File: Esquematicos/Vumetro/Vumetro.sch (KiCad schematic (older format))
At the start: 13 parts

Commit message: actualización esquemático matriz de led y driver
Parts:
- removed J?: AudioJack3_Ground, symbol Connector:AudioJack3_Ground
- added C?: 1.0uF, symbol pspice:CAP
- added C?: 0.1uF, symbol pspice:CAP
- added J?: AudioJack5_Ground, symbol Connector:AudioJack5_Ground
- added R?: 10K, symbol Device:R
- U?: symbol vumetro:MAX7219 -> Vumetro-rescue:MAX7219-vumetro
- U? (x2): symbol vumetro:conn_pin8 -> Vumetro-rescue:conn_pin8-vumetro
- U?: symbol vumetro:opa2350pa -> Vumetro-rescue:opa2350pa-vumetro
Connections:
- net labels added: +5V, DIC0, DIC1, DIC2, DIC3, DIC4, DIC5, DIC6, DIC7, GND, ISET, SEGA, SEGB, SEGC, SEGD, SEGDP, SEGE, SEGF, SEGG, SPI_MOSI, SPI_SCK, V+
- wire segments 33 -> 105
- no-connect marks 4 -> 9
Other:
- moved on the sheet: C1, C2, R1, R2, R?, RV?, U?

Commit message: esquematico final
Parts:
- removed U?: MAX7219, symbol Vumetro-rescue:MAX7219-vumetro
- added P1, P2: conn_pin40, symbol vumetro:conn_pin40
- added U1: MAX7219, symbol vumetro:MAX7219
- U2, U3: renamed from U?; symbol Vumetro-rescue:conn_pin8-vumetro -> Vumetro-rescue:conn_pin8-vumetro-Vumetro-rescue
- U4: renamed from U?; symbol Vumetro-rescue:opa2350pa-vumetro -> Vumetro-rescue:opa2350pa-vumetro-Vumetro-rescue
- gave numbers to parts that had none: 8
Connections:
- net labels added: 3V3, 5V, CH1, VCC
- net labels removed: ADC
- wire segments 105 -> 136
- no-connect marks 9 -> 55

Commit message: perdon capitan
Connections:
- net labels added: +3V3
- net labels removed: +3.3V, VCC
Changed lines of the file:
@@
 $EndComp
-$Comp
-L power:+3.3V #PWR0101
-U 1 1 5BD083BF
-P 3350 2050
-F 0 "#PWR0101" H 3350 1900 50  0001 C CNN
-F 1 "+3.3V" H 3365 2223 50  0000 C CNN
-F 2 "" H 3350 2050 50  0001 C CNN
-F 3 "" H 3350 2050 50  0001 C CNN
-	1    3350 2050
-	1    0    0    -1
-$EndComp
-Wire Wire Line
-	3350 2050 3350 2250
 $Comp
 L power:GNDA #PWR0102
@@
 	1    0    0    -1
 $EndComp
-$Comp
-L power:GND #PWR0110
-U 1 1 5C0A259B
-P 1050 1900
-F 0 "#PWR0110" H 1050 1650 50  0001 C CNN
-F 1 "GND" H 1055 1727 50  0000 C CNN
-F 2 "" H 1050 1900 50  0001 C CNN
-F 3 "" H 1050 1900 50  0001 C CNN
-	1    1050 1900
-	1    0    0    -1
-$EndComp
-$Comp
-L power:PWR_FLAG #FLG0102
-U 1 1 5C0A2919
-P 1500 1900
-F 0 "#FLG0102" H 1500 1975 50  0001 C CNN
-F 1 "PWR_FLAG" H 1500 2073 50  0000 C CNN
-F 2 "" H 1500 1900 50  0001 C CNN
-F 3 "~" H 1500 1900 50  0001 C CNN
-	1    1500 1900
-	1    0    0    -1
-$EndComp
-$Comp
-L power:VCC #PWR0111
-U 1 1 5C0A2E53
-P 1500 1900
-F 0 "#PWR0111" H 1500 1750 50  0001 C CNN
-F 1 "VCC" H 1517 2073 50  0000 C CNN
-F 2 "" H 1500 1900 50  0001 C CNN
-F 3 "" H 1500 1900 50  0001 C CNN
-	1    1500 1900
-	-1   0    0    1
-$EndComp
 Wire Wire Line
 	2200 5450 1900 5450
@@
 	1    0    0    -1
 $EndComp
+Wire Wire Line
+	3350 2250 3350 2050
+$Comp
+L power:PWR_FLAG #FLG0102
+U 1 1 5BDCD5F1
+P 1050 3000
+F 0 "#FLG0102" H 1050 3075 50  0001 C CNN
+F 1 "PWR_FLAG" H 1050 3173 50  0000 C CNN
+F 2 "" H 1050 3000 50  0001 C CNN
+F 3 "~" H 1050 3000 50  0001 C CNN
+	1    1050 3000
+	1    0    0    -1
+$EndComp
+$Comp
+L power:+3V3 #PWR0101
+U 1 1 5BDC0419
+P 1050 3000
+F 0 "#PWR0101" H 1050 2850 50  0001 C CNN
+F 1 "+3V3" H 1065 3173 50  0000 C CNN
+F 2 "" H 1050 3000 50  0001 C CNN
+F 3 "" H 1050 3000 50  0001 C CNN
+	1    1050 3000
+	-1   0    0    1
+$EndComp
+Text Label 3350 2050 0    50   ~ 0
++3V3
+$Comp
+L power:GNDA #PWR0110
+U 1 1 5BE11156
+P 1050 1900
+F 0 "#PWR0110" H 1050 1650 50  0001 C CNN
+F 1 "GNDA" H 1055 1727 50  0000 C CNN
+F 2 "" H 1050 1900 50  0001 C CNN
+F 3 "" H 1050 1900 50  0001 C CNN
+	1    1050 1900
+	1    0    0    -1
+$EndComp
+$Comp
+L power:PWR_FLAG #FLG0103
+U 1 1 5BE11DF9
+P 1050 2450
+F 0 "#FLG0103" H 1050 2525 50  0001 C CNN
+F 1 "PWR_FLAG" H 1050 2623 50  0000 C CNN
+F 2 "" H 1050 2450 50  0001 C CNN
+F 3 "~" H 1050 2450 50  0001 C CNN
+	1    1050 2450
+	1    0    0    -1
+$EndComp
+$Comp
+L power:+5V #PWR0111
+U 1 1 5BE126C5
+P 1050 2450
+F 0 "#PWR0111" H 1050 2300 50  0001 C CNN
+F 1 "+5V" H 1065 2623 50  0000 C CNN
+F 2 "" H 1050 2450 50  0001 C CNN
+F 3 "" H 1050 2450 50  0001 C CNN
+	1    1050 2450
+	-1   0    0    1
+$EndComp
 $EndSCHEMATC

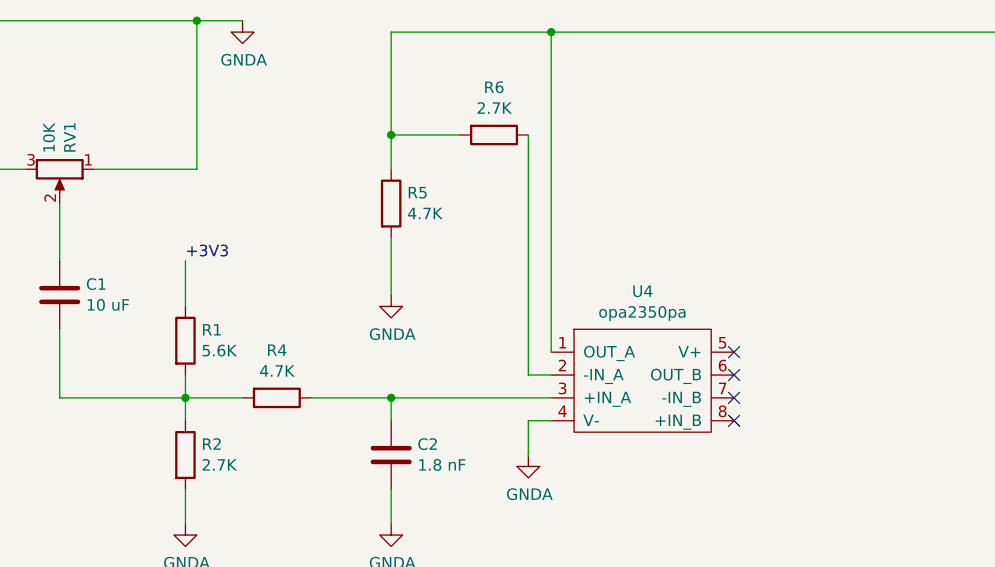
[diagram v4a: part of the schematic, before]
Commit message: correccion esquematico
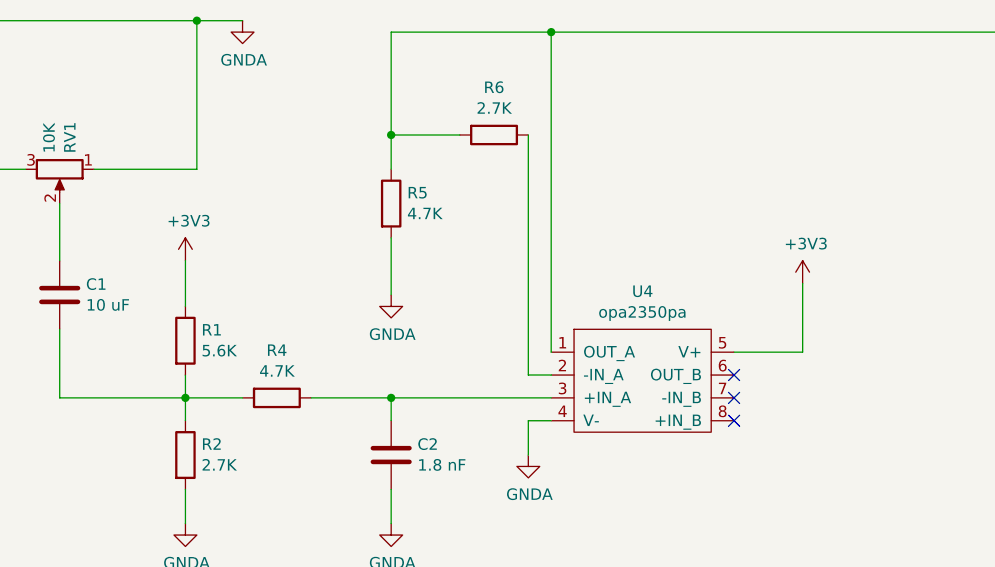
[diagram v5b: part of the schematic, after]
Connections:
- wire segments 136 -> 138
- no-connect marks 55 -> 54
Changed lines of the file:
@@
 Wire Wire Line
 	4850 2750 4950 2750
-NoConn ~ 5750 2450
 NoConn ~ 5750 2550
 NoConn ~ 5750 2650
@@
 	1    0    0    -1
 $EndComp
-Wire Wire Line
-	3350 2250 3350 2050
 $Comp
 L power:PWR_FLAG #FLG0102
@@
 	1    0    0    -1
 $EndComp
+$Comp
+L power:GNDA #PWR0110
+U 1 1 5BE11156
+P 1050 1900
+F 0 "#PWR0110" H 1050 1650 50  0001 C CNN
+F 1 "GNDA" H 1055 1727 50  0000 C CNN
+F 2 "" H 1050 1900 50  0001 C CNN
+F 3 "" H 1050 1900 50  0001 C CNN
+	1    1050 1900
+	1    0    0    -1
+$EndComp
+$Comp
+L power:PWR_FLAG #FLG0103
+U 1 1 5BE11DF9
+P 1050 2450
+F 0 "#FLG0103" H 1050 2525 50  0001 C CNN
+F 1 "PWR_FLAG" H 1050 2623 50  0000 C CNN
+F 2 "" H 1050 2450 50  0001 C CNN
+F 3 "~" H 1050 2450 50  0001 C CNN
+	1    1050 2450
+	1    0    0    -1
+$EndComp
+$Comp
+L power:+5V #PWR0111
+U 1 1 5BE126C5
+P 1050 2450
+F 0 "#PWR0111" H 1050 2300 50  0001 C CNN
+F 1 "+5V" H 1065 2623 50  0000 C CNN
+F 2 "" H 1050 2450 50  0001 C CNN
+F 3 "" H 1050 2450 50  0001 C CNN
+	1    1050 2450
+	-1   0    0    1
+$EndComp
+Wire Wire Line
+	3350 2250 3350 2050
+$Comp
+L power:+3V3 #PWR0112
+U 1 1 5BDC2B19
+P 3350 2050
+F 0 "#PWR0112" H 3350 1900 50  0001 C CNN
+F 1 "+3V3" H 3365 2223 50  0000 C CNN
+F 2 "" H 3350 2050 50  0001 C CNN
+F 3 "" H 3350 2050 50  0001 C CNN
+	1    3350 2050
+	1    0    0    -1
+$EndComp
+Wire Wire Line
+	5750 2450 6050 2450
 $Comp
 L power:+3V3 #PWR0101
@@
 	-1   0    0    1
 $EndComp
-Text Label 3350 2050 0    50   ~ 0
-+3V3
-$Comp
-L power:GNDA #PWR0110
-U 1 1 5BE11156
-P 1050 1900
-F 0 "#PWR0110" H 1050 1650 50  0001 C CNN
-F 1 "GNDA" H 1055 1727 50  0000 C CNN
-F 2 "" H 1050 1900 50  0001 C CNN
-F 3 "" H 1050 1900 50  0001 C CNN
-	1    1050 1900
-	1    0    0    -1
-$EndComp
-$Comp
-L power:PWR_FLAG #FLG0103
-U 1 1 5BE11DF9
-P 1050 2450
-F 0 "#FLG0103" H 1050 2525 50  0001 C CNN
-F 1 "PWR_FLAG" H 1050 2623 50  0000 C CNN
-F 2 "" H 1050 2450 50  0001 C CNN
-F 3 "~" H 1050 2450 50  0001 C CNN
-	1    1050 2450
-	1    0    0    -1
-$EndComp
-$Comp
-L power:+5V #PWR0111
-U 1 1 5BE126C5
-P 1050 2450
-F 0 "#PWR0111" H 1050 2300 50  0001 C CNN
-F 1 "+5V" H 1065 2623 50  0000 C CNN
-F 2 "" H 1050 2450 50  0001 C CNN
-F 3 "" H 1050 2450 50  0001 C CNN
-	1    1050 2450
-	-1   0    0    1
-$EndComp
+$Comp
+L power:+3V3 #PWR0113
+U 1 1 5BDD5FCB
+P 6050 2150
+F 0 "#PWR0113" H 6050 2000 50  0001 C CNN
+F 1 "+3V3" H 6065 2323 50  0000 C CNN
+F 2 "" H 6050 2150 50  0001 C CNN
+F 3 "" H 6050 2150 50  0001 C CNN
+	1    6050 2150
+	1    0    0    -1
+$EndComp
+Wire Wire Line
+	6050 2150 6050 2450
 $EndSCHEMATC

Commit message: actualización del esquemático se agregar el teclado.
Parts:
- added J2: Conn_Teclado_Matricial_4x4, symbol Connector:Conn_01x08_Female
- C1, C2: symbol Device:C -> Vumetro-rescue:C-Device
- C3, C4: symbol pspice:CAP -> Vumetro-rescue:CAP-pspice
- J1: symbol Connector:AudioJack5_Ground -> Vumetro-rescue:AudioJack5_Ground-Connector
- P1, P2: symbol vumetro:conn_pin40 -> Vumetro-rescue:conn_pin40-vumetro
- R1, R2, R3, R4, R5, R6: symbol Device:R -> Vumetro-rescue:R-Device
- RV1: symbol Device:R_POT -> Vumetro-rescue:R_POT-Device
- U1: symbol vumetro:MAX7219 -> Vumetro-rescue:MAX7219-vumetro
- U2, U3: symbol Vumetro-rescue:conn_pin8-vumetro-Vumetro-rescue -> Vumetro-rescue:conn_pin8-vumetro-Vumetro-rescue-Vumetro-rescue
- U4: symbol Vumetro-rescue:opa2350pa-vumetro-Vumetro-rescue -> Vumetro-rescue:opa2350pa-vumetro-Vumetro-rescue-Vumetro-rescue
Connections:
- net labels added: 232_TX, CAN_RD, CAN_TD, T_COL0, T_COL1, T_FIL0, T_FIL2, T_FIL3
- wire segments 138 -> 154
- no-connect marks 54 -> 46
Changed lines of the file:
@@
 EESchema Schematic File Version 4
 LIBS:Vumetro-cache
-EELAYER 29 0
+EELAYER 26 0
 EELAYER END
 $Descr A4 11693 8268
@@
 $EndDescr
 $Comp
-L Device:R R1
+L Vumetro-rescue:R-Device R1
 U 1 1 5BD08240
 P 3350 2400
@@
 $EndComp
 $Comp
-L Device:R R2
+L Vumetro-rescue:R-Device R2
 U 1 1 5BD082FA
 P 3350 2900
@@
 $EndComp
 $Comp
-L power:GNDA #PWR0102
+L Vumetro-rescue:GNDA-power #PWR0102
 U 1 1 5BD08B01
 P 3600 1000
@@
 	2400 1400 1950 1400
 $Comp
-L Device:R_POT RV1
+L Vumetro-rescue:R_POT-Device RV1
 U 1 1 5BD09203
 P 2800 1650
@@
 Connection ~ 3350 2650
 $Comp
-L power:GNDA #PWR0103
+L Vumetro-rescue:GNDA-power #PWR0103
 U 1 1 5BD0D7F2
 P 3350 3200
@@
 $EndComp
 $Comp
-L Device:C C2
+L Vumetro-rescue:C-Device C2
 U 1 1 5BD1B29A
 P 4250 2900
@@
 $EndComp
 $Comp
-L power:GNDA #PWR0104
+L Vumetro-rescue:GNDA-power #PWR0104
 U 1 1 5BD1B343
 P 4250 3200
@@
 	4250 3050 4250 3200
 $Comp
-L Device:R R4
+L Vumetro-rescue:R-Device R4
 U 1 1 5BD1B49E
 P 3750 2650
@@
 Connection ~ 4250 2650
 $Comp
-L Device:R R5
+L Vumetro-rescue:R-Device R5
 U 1 1 5BD1FFCF
 P 4250 1800
@@
 $EndComp
 $Comp
-L Device:R R6
+L Vumetro-rescue:R-Device R6
 U 1 1 5BD204D6
 P 4700 1500
@@
 	4250 1500 4250 1650
 $Comp
-L power:GNDA #PWR0105
+L Vumetro-rescue:GNDA-power #PWR0105
 U 1 1 5BD20C9D
 P 4250 2200
@@
 	4250 1950 4250 2200
 $Comp
-L Device:C C1
+L Vumetro-rescue:C-Device C1
 U 1 1 5BD214BE
 P 2800 2200
@@
 CH1
 $Comp
-L Vumetro-rescue:conn_pin8-vumetro-Vumetro-rescue U2
+L Vumetro-rescue:conn_pin8-vumetro-Vumetro-rescue-Vumetro-rescue U2
 U 1 1 5BD8D993
 P 4200 3850
@@
 $EndComp
 $Comp
-L Vumetro-rescue:conn_pin8-vumetro-Vumetro-rescue U3
+L Vumetro-rescue:conn_pin8-vumetro-Vumetro-rescue-Vumetro-rescue U3
 U 1 1 5BD8E115
 P 4650 3850
@@
 $EndComp
 $Comp
-L Vumetro-rescue:opa2350pa-vumetro-Vumetro-rescue U4
+L Vumetro-rescue:opa2350pa-vumetro-Vumetro-rescue-Vumetro-rescue U4
 U 1 1 5BD9369A
 P 5350 2250
@@
 	4250 1050 4250 1500
 $Comp
-L power:GNDA #PWR0106
+L Vumetro-rescue:GNDA-power #PWR0106
 U 1 1 5BD9D42A
 P 4850 2900
@@
 ISET
 $Comp
-L pspice:CAP C4
+L Vumetro-rescue:CAP-pspice C4
 U 1 1 5BDF9589
 P 4900 6800
@@
 $EndComp
 $Comp
-L pspice:CAP C3
+L Vumetro-rescue:CAP-pspice C3
 U 1 1 5BDF96A7
 P 4300 6800
@@
 $EndComp
 $Comp
-L Device:R R3
+L Vumetro-rescue:R-Device R3
 U 1 1 5BDF9744
 P 3600 7050
@@
 $EndComp
 $Comp
-L power:GNDA #PWR0107
+L Vumetro-rescue:GNDA-power #PWR0107
 U 1 1 5BDF9885
 P 4300 7150
@@
 $EndComp
 $Comp
-L power:+5V #PWR0108
+L Vumetro-rescue:+5V-power #PWR0108
 U 1 1 5BDFBFF0
 P 3800 6550
@@
 $EndComp
 $Comp
-L power:GNDA #PWR0109
+L Vumetro-rescue:GNDA-power #PWR0109
 U 1 1 5BDFC0B2
 P 4900 7150
@@
 NoConn ~ 3200 5250
 $Comp
-L Connector:AudioJack5_Ground J1
+L Vumetro-rescue:AudioJack5_Ground-Connector J1
 U 1 1 5BE5F8BB
 P 1750 1200
@@
 NoConn ~ 1950 1100
 $Comp
-L vumetro:conn_pin40 P2
+L Vumetro-rescue:conn_pin40-vumetro P2
 U 1 1 5BD92927
 P 8250 2750
@@
 $EndComp
 $Comp
-L vumetro:conn_pin40 P1
+L Vumetro-rescue:conn_pin40-vumetro P1
 U 1 1 5BD936AB
 P 9700 2750
@@
 NoConn ~ 9450 3850
 NoConn ~ 9450 3950
-NoConn ~ 9450 4850
-NoConn ~ 9450 4750
-NoConn ~ 9450 4650
-NoConn ~ 9450 4550
-NoConn ~ 9450 4450
-NoConn ~ 9450 4350
-NoConn ~ 9450 4250
-NoConn ~ 9450 4150
 NoConn ~ 9450 4050
 Text Label 7650 2950 0    50   ~ 0
@@
 	4950 1050 4950 2450
 $Comp
-L power:PWR_FLAG #FLG0101
+L Vumetro-rescue:PWR_FLAG-power #FLG0101
 U 1 1 5C0A1FED
 P 1050 1900
@@
 DIC7
 $Comp
-L vumetro:MAX7219 U1
+L Vumetro-rescue:MAX7219-vumetro U1
 U 1 1 5BD94EE9
 P 2700 5150
@@
 $EndComp
 $Comp
-L power:PWR_FLAG #FLG0102
+L Vumetro-rescue:PWR_FLAG-power #FLG0102
 U 1 1 5BDCD5F1
 P 1050 3000
@@
 $EndComp
 $Comp
-L power:GNDA #PWR0110
+L Vumetro-rescue:GNDA-power #PWR0110
 U 1 1 5BE11156
 P 1050 1900
@@
 $EndComp
 $Comp
-L power:PWR_FLAG #FLG0103
+L Vumetro-rescue:PWR_FLAG-power #FLG0103
 U 1 1 5BE11DF9
 P 1050 2450
@@
 $EndComp
 $Comp
-L power:+5V #PWR0111
+L Vumetro-rescue:+5V-power #PWR0111
 U 1 1 5BE126C5
 P 1050 2450
@@
 	3350 2250 3350 2050
 $Comp
-L power:+3V3 #PWR0112
+L Vumetro-rescue:+3V3-power #PWR0112
 U 1 1 5BDC2B19
 P 3350 2050
@@
 	5750 2450 6050 2450
 $Comp
-L power:+3V3 #PWR0101
+L Vumetro-rescue:+3V3-power #PWR0101
 U 1 1 5BDC0419
 P 1050 3000
@@
 $EndComp
 $Comp
-L power:+3V3 #PWR0113
+L Vumetro-rescue:+3V3-power #PWR0113
 U 1 1 5BDD5FCB
 P 6050 2150
@@
 Wire Wire Line
 	6050 2150 6050 2450
+$Comp
+L Connector:Conn_01x08_Female J2
+U 1 1 5BEC2E1E
+P 9050 1850
+F 0 "J2" H 8700 2500 50  0000 L CNN
+F 1 "Conn_Teclado_Matricial_4x4" H 8350 2350 50  0000 L CNN
+F 2 "" H 9050 1850 50  0001 C CNN
+F 3 "~" H 9050 1850 50  0001 C CNN
+	1    9050 1850
+	1    0    0    -1
+$EndComp
+Wire Wire Line
+	8850 1550 8650 1550
+Wire Wire Line
+	8850 1650 8650 1650
+Wire Wire Line
+	8850 1750 8650 1750
+Wire Wire Line
+	8850 1850 8650 1850
+Wire Wire Line
+	8850 1950 8650 1950
+Wire Wire Line
+	8850 2050 8650 2050
+Wire Wire Line
+	8850 2150 8650 2150
+Wire Wire Line
+	8850 2250 8650 2250
+Text Label 8650 1550 2    50   ~ 0
+232_TX
+Text Label 8650 1650 2    50   ~ 0
+CAN_RD
+Text Label 8650 1750 2    50   ~ 0
+CAN_TD
+Text Label 8650 1850 2    50   ~ 0
+T_COL1
+Text Label 8650 1950 2    50   ~ 0
+T_FIL0
+Text Label 8650 2050 2    50   ~ 0
+T_FIL3
+Text Label 8650 2150 2    50   ~ 0
+T_FIL2
+Text Label 8650 2250 2    50   ~ 0
+T_COL0
+Wire Wire Line
+	9250 4850 9450 4850
+Wire Wire Line
+	9450 4750 9250 4750
+Wire Wire Line
+	9450 4650 9250 4650
+Wire Wire Line
+	9450 4550 9250 4550
+Wire Wire Line
+	9450 4450 9250 4450
+Wire Wire Line
+	9450 4350 9250 4350
+Wire Wire Line
+	9450 4250 9250 4250
+Wire Wire Line
+	9450 4150 9250 4150
+Text Label 9250 4850 2    50   ~ 0
+T_COL0
+Text Label 9250 4750 2    50   ~ 0
+T_FIL2
+Text Label 9250 4650 2    50   ~ 0
+T_FIL3
+Text Label 9250 4550 2    50   ~ 0
+T_FIL0
+Text Label 9250 4450 2    50   ~ 0
+T_COL1
+Text Label 9250 4350 2    50   ~ 0
+CAN_TD
+Text Label 9250 4250 2    50   ~ 0
+CAN_RD
+Text Label 9250 4150 2    50   ~ 0
+232_TX
 $EndSCHEMATC
